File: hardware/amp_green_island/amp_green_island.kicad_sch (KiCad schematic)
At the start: 0 parts

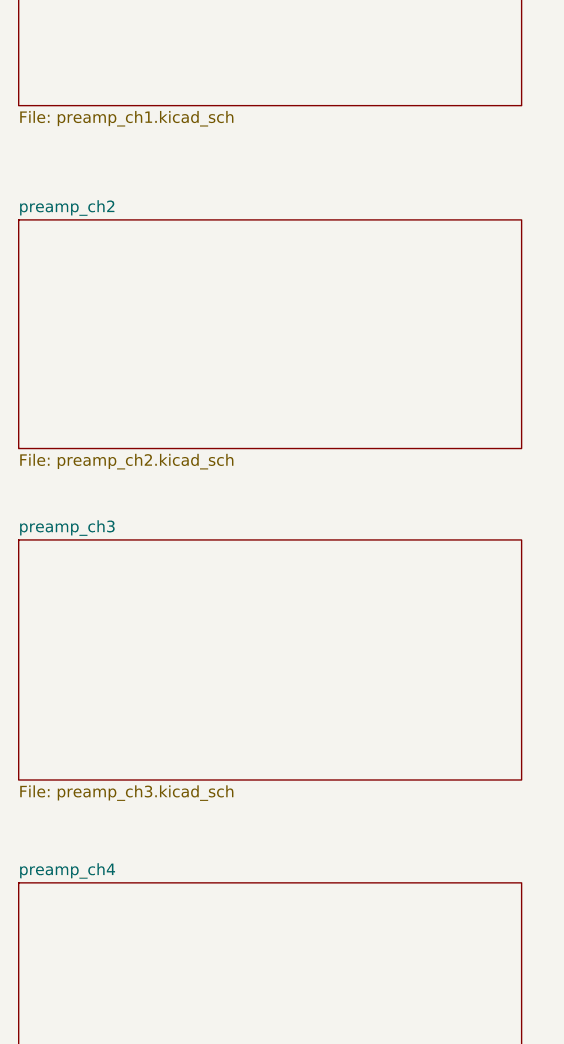
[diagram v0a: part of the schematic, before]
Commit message: amp_green_island: add all 4 channels to schematic
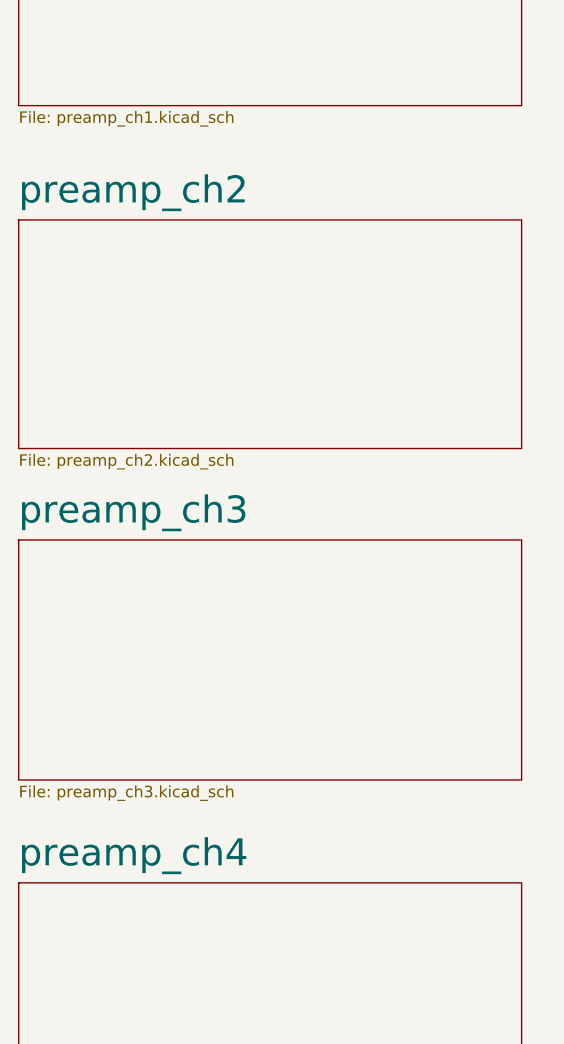
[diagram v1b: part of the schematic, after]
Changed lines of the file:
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@@
     (stroke (width 0.1524) (type solid))
     (fill (color 0 0 0 0.0000))
-    (property "Sheetname" "preamp_ch4" (at 48.26 142.7984 0)
-      (effects (font (size 1.27 1.27)) (justify left bottom))
+    (property "Sheetname" "preamp_ch4" (at 48.26 141.9334 0)
+      (effects (font (size 3 3)) (justify left bottom))
     )
     (property "Sheetfile" "preamp_ch4.kicad_sch" (at 48.26 169.4946 0)
@@
     (stroke (width 0.1524) (type solid))
     (fill (color 0 0 0 0.0000))
-    (property "Sheetname" "preamp_ch2" (at 48.26 69.1384 0)
-      (effects (font (size 1.27 1.27)) (justify left bottom))
+    (property "Sheetname" "preamp_ch2" (at 48.26 68.2734 0)
+      (effects (font (size 3 3)) (justify left bottom))
     )
     (property "Sheetfile" "preamp_ch2.kicad_sch" (at 48.26 95.8346 0)
@@
     (stroke (width 0.1524) (type solid))
     (fill (color 0 0 0 0.0000))
-    (property "Sheetname" "preamp_ch3" (at 48.26 104.6984 0)
-      (effects (font (size 1.27 1.27)) (justify left bottom))
+    (property "Sheetname" "preamp_ch3" (at 48.26 103.8334 0)
+      (effects (font (size 3 3)) (justify left bottom))
     )
     (property "Sheetfile" "preamp_ch3.kicad_sch" (at 48.26 132.6646 0)

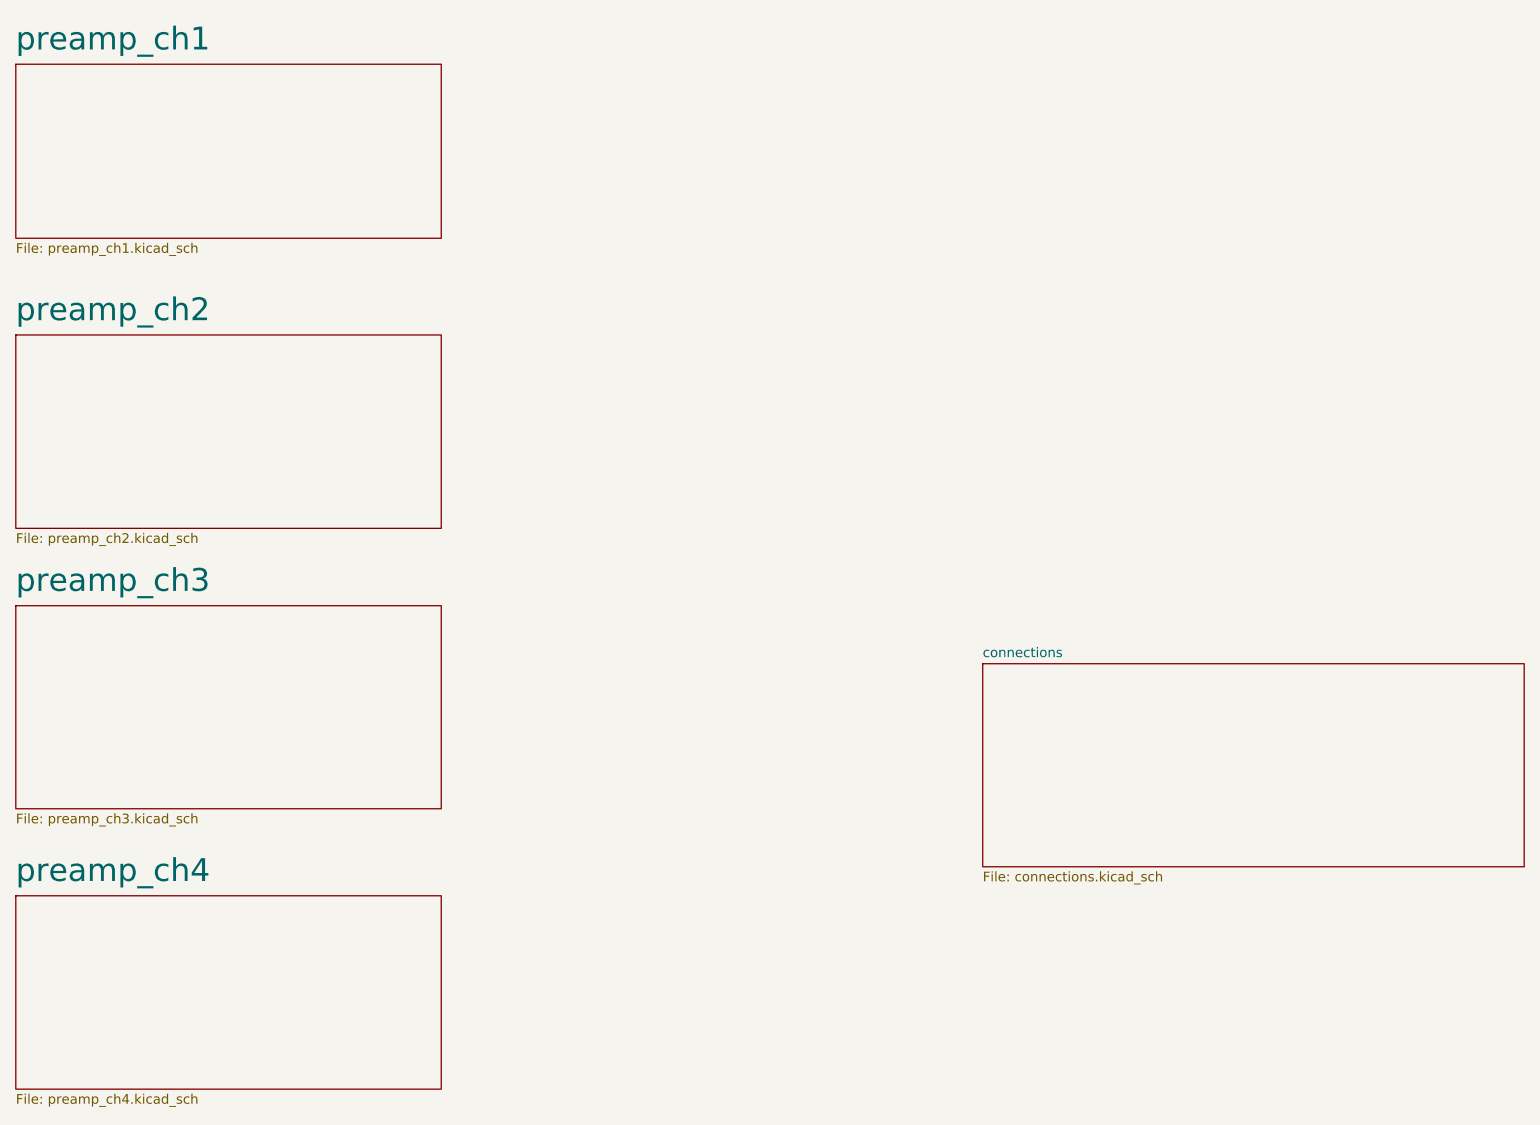
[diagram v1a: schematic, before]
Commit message: green_island: pcb routing done
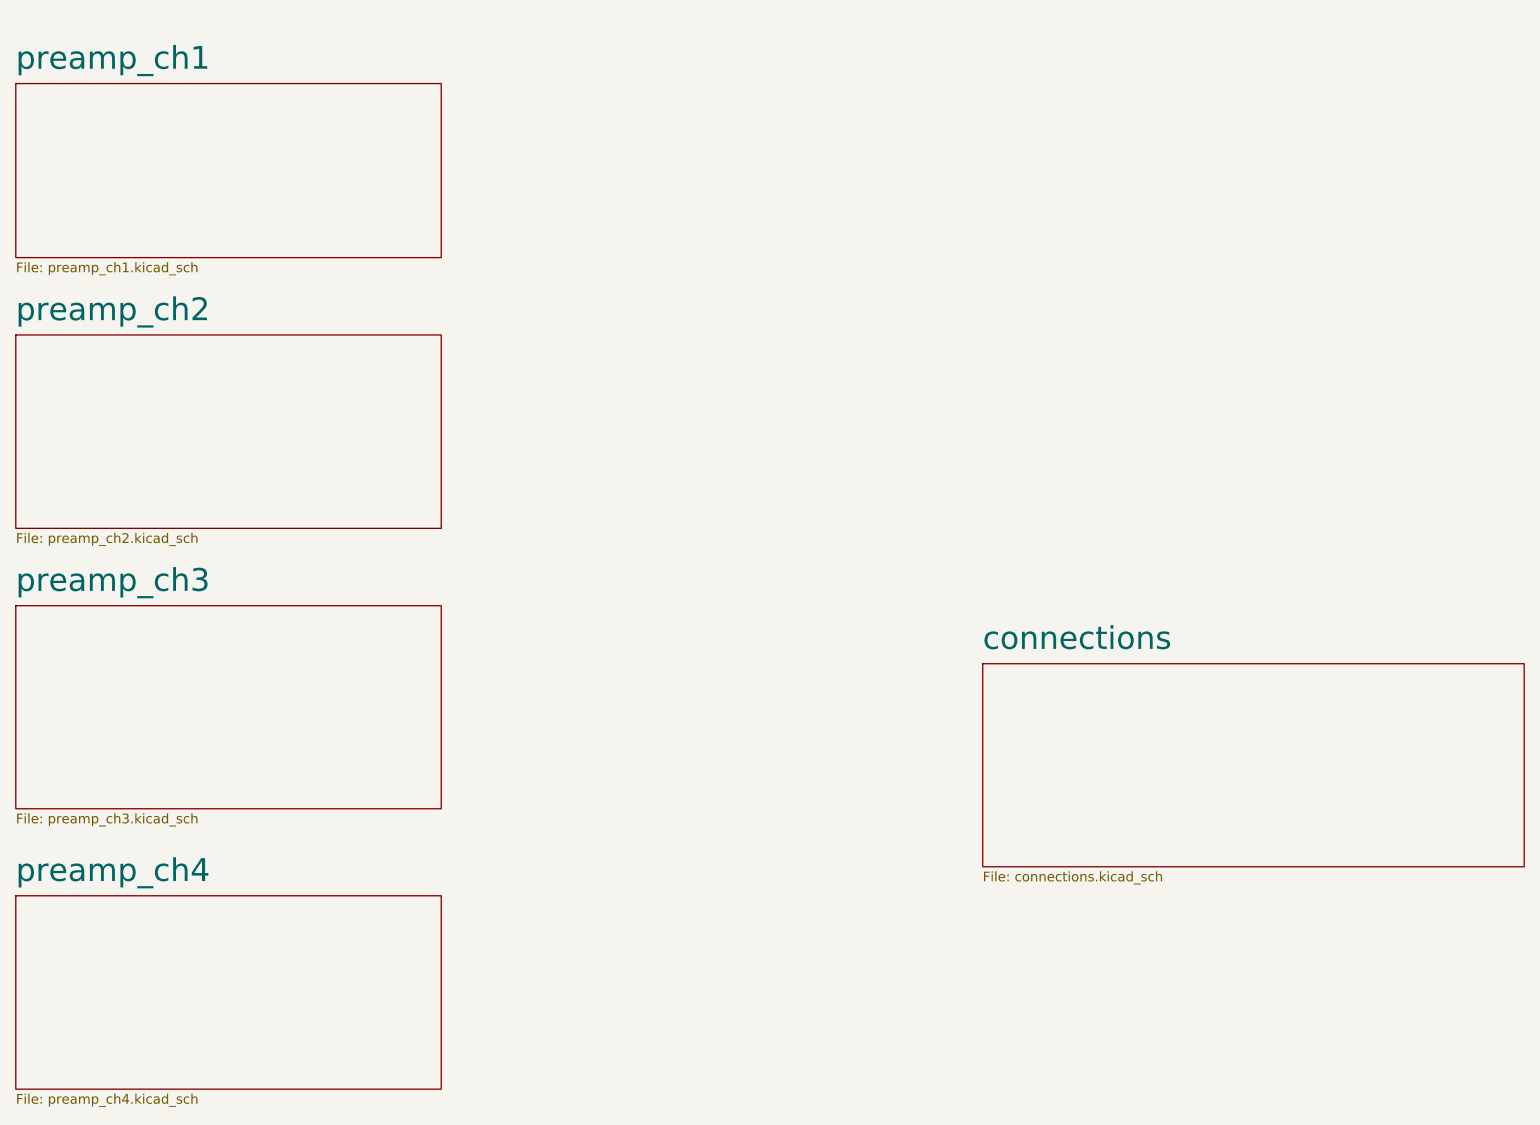
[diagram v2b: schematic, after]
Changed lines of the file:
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@@
     (stroke (width 0.1524) (type solid))
     (fill (color 0 0 0 0.0000))
-    (property "Sheetname" "connections" (at 175.26 112.3184 0)
-      (effects (font (size 1.27 1.27)) (justify left bottom))
+    (property "Sheetname" "connections" (at 175.26 111.4534 0)
+      (effects (font (size 3 3)) (justify left bottom))
     )
     (property "Sheetfile" "connections.kicad_sch" (at 175.26 140.2846 0)
@@
     )
   )
-  (sheet (at 48.26 34.29) (size 55.88 22.86) (fields_autoplaced)
+  (sheet (at 48.26 36.83) (size 55.88 22.86) (fields_autoplaced)
     (stroke (width 0.1524) (type solid))
     (fill (color 0 0 0 0.0000))
-    (property "Sheetname" "preamp_ch1" (at 48.26 32.7134 0)
+    (property "Sheetname" "preamp_ch1" (at 48.26 35.2534 0)
       (effects (font (size 3 3)) (justify left bottom))
     )
-    (property "Sheetfile" "preamp_ch1.kicad_sch" (at 48.26 57.7346 0)
+    (property "Sheetfile" "preamp_ch1.kicad_sch" (at 48.26 60.2746 0)
       (effects (font (size 1.27 1.27)) (justify left top))
     )
